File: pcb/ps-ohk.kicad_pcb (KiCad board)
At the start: 2 copper layers, 17 parts, among them IC1 CH552G

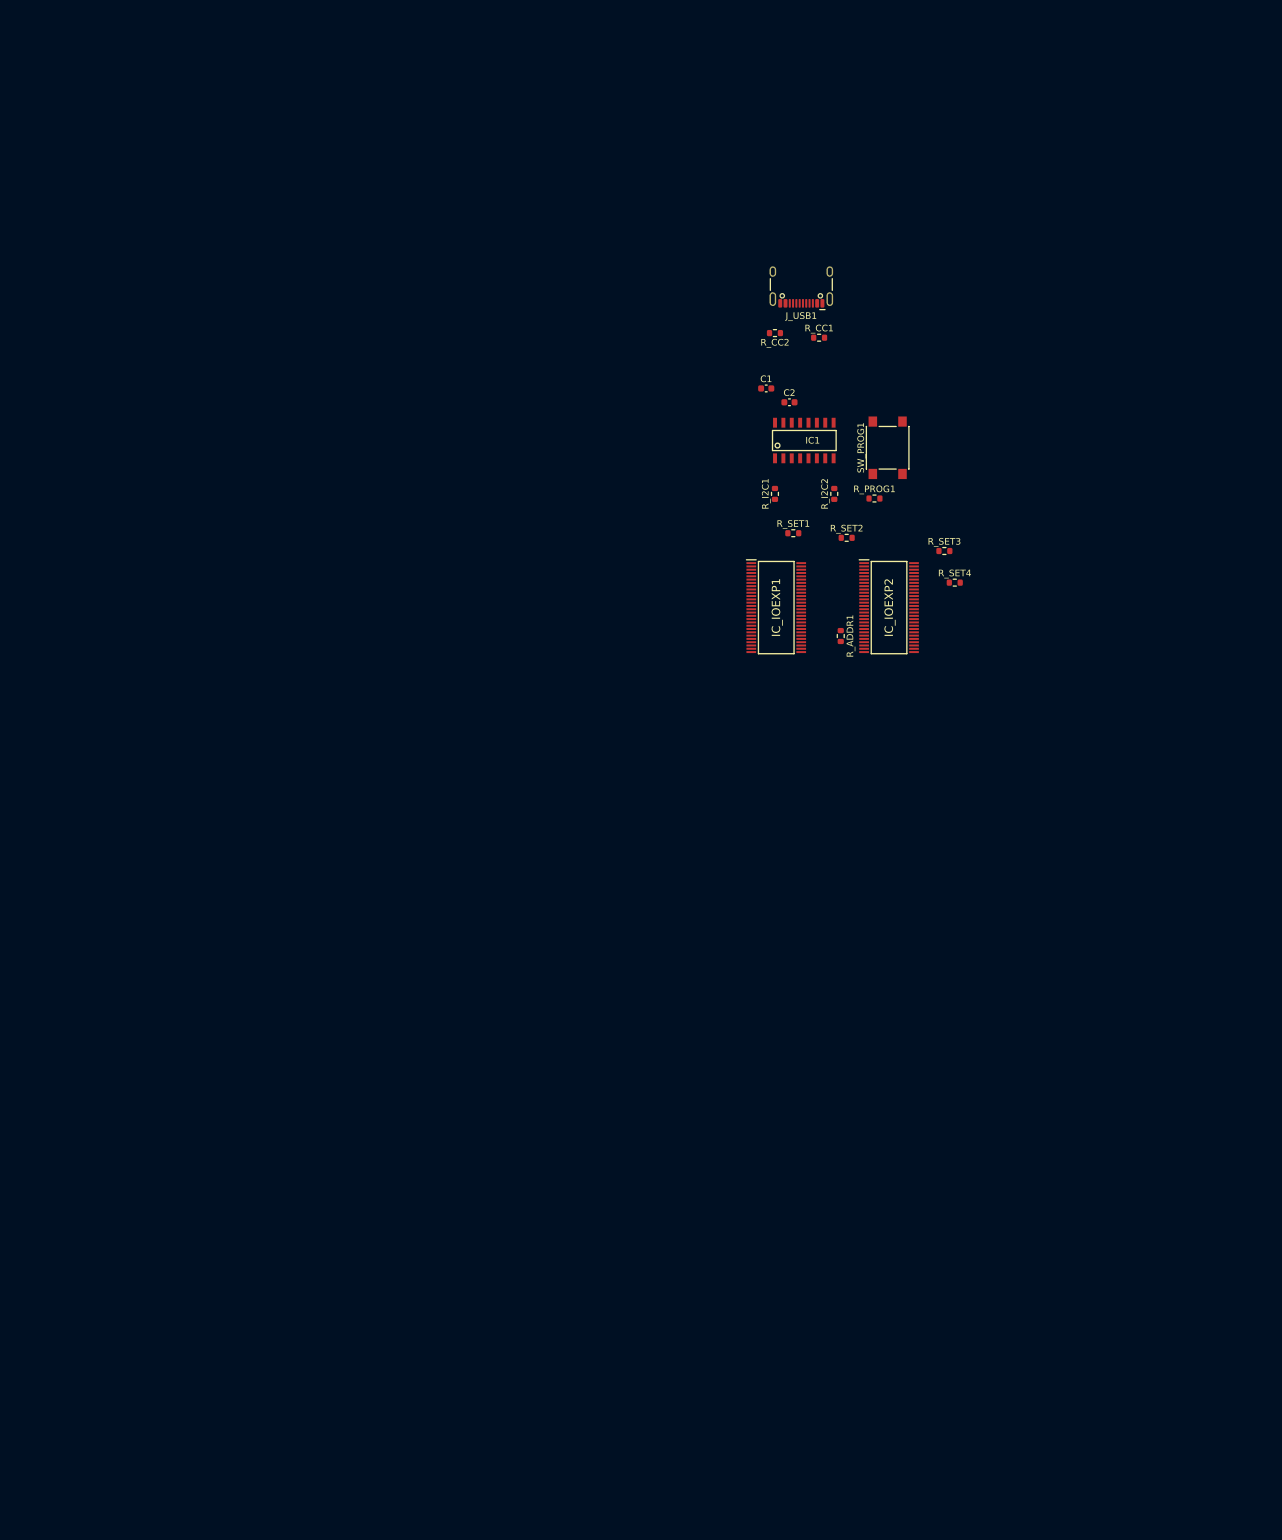
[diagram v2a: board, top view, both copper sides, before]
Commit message: pcb: add buttons and route
Signed-off-by: Dylan Turner <dylan.turner@tutanota.com>
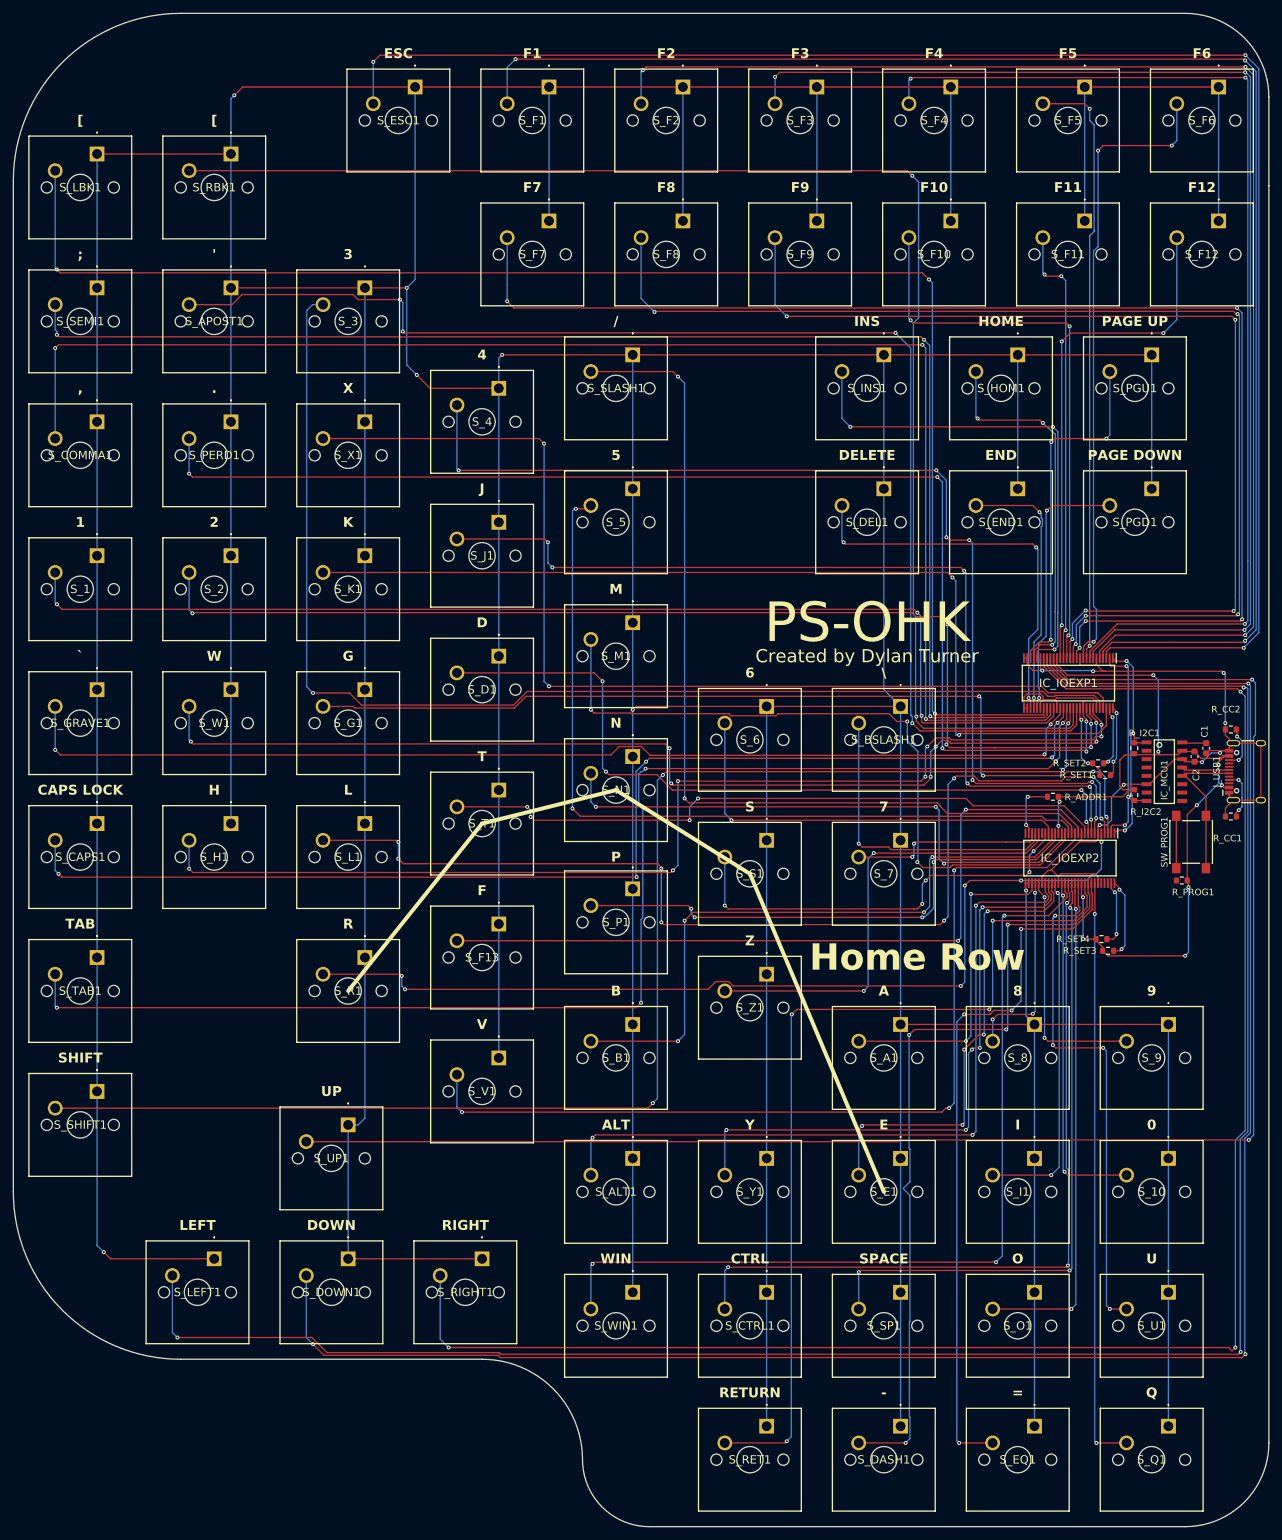
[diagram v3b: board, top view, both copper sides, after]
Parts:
- added S_1: ~, COM-13834:COM13834, F.Cu at (27.9, 81.3)
- added S_10: ~, COM-13834:COM13834, F.Cu at (190.5, 172.7)
- added S_2: ~, COM-13834:COM13834, F.Cu at (48.3, 81.3)
- added S_3: ~, COM-13834:COM13834, F.Cu at (68.6, 40.6)
- added S_4: ~, COM-13834:COM13834, F.Cu at (88.9, 55.9)
- added S_5: ~, COM-13834:COM13834, F.Cu at (109.2, 71.1)
- added S_6: ~, COM-13834:COM13834, F.Cu at (129.5, 104.1)
- added S_7: ~, COM-13834:COM13834, F.Cu at (149.9, 124.5)
- added S_8: ~, COM-13834:COM13834, F.Cu at (170.2, 152.4)
- added S_9: ~, COM-13834:COM13834, F.Cu at (190.5, 152.4)
- added S_A1: ~, COM-13834:COM13834, F.Cu at (149.9, 152.4)
- added S_ALT1: ~, COM-13834:COM13834, F.Cu at (109.2, 172.7)
- added S_APOST1: ~, COM-13834:COM13834, F.Cu at (48.3, 40.6)
- added S_B1: ~, COM-13834:COM13834, F.Cu at (109.2, 152.4)
- added S_BSLASH1: ~, COM-13834:COM13834, F.Cu at (149.9, 104.1)
- added S_CAPS1: ~, COM-13834:COM13834, F.Cu at (27.9, 121.9)
- added S_COMMA1: ~, COM-13834:COM13834, F.Cu at (27.9, 61.0)
- added S_CTRL1: ~, COM-13834:COM13834, F.Cu at (129.5, 193.0)
- added S_D1: ~, COM-13834:COM13834, F.Cu at (88.9, 96.5)
- added S_DASH1: ~, COM-13834:COM13834, F.Cu at (149.9, 213.4)
- added S_DEL1: ~, COM-13834:COM13834, F.Cu at (147.3, 71.1)
- added S_DOWN1: ~, COM-13834:COM13834, F.Cu at (66.0, 188.0)
- added S_E1: ~, COM-13834:COM13834, F.Cu at (149.9, 172.7)
- added S_END1: ~, COM-13834:COM13834, F.Cu at (167.6, 71.1)
- added S_EQ1: ~, COM-13834:COM13834, F.Cu at (170.2, 213.4)
- added S_ESC1: ~, COM-13834:COM13834, F.Cu at (76.2, 10.2)
- added S_F1: ~, COM-13834:COM13834, F.Cu at (96.5, 10.2)
- added S_F10: ~, COM-13834:COM13834, F.Cu at (157.5, 30.5)
- added S_F11: ~, COM-13834:COM13834, F.Cu at (177.8, 30.5)
- added S_F12: ~, COM-13834:COM13834, F.Cu at (198.1, 30.5)
- added S_F13: ~, COM-13834:COM13834, F.Cu at (88.9, 137.2)
- added S_F2: ~, COM-13834:COM13834, F.Cu at (116.8, 10.2)
- added S_F3: ~, COM-13834:COM13834, F.Cu at (137.2, 10.2)
- added S_F4: ~, COM-13834:COM13834, F.Cu at (157.5, 10.2)
- added S_F5: ~, COM-13834:COM13834, F.Cu at (177.8, 10.2)
- added S_F6: ~, COM-13834:COM13834, F.Cu at (198.1, 10.2)
- added S_F7: ~, COM-13834:COM13834, F.Cu at (96.5, 30.5)
- added S_F8: ~, COM-13834:COM13834, F.Cu at (116.8, 30.5)
- added S_F9: ~, COM-13834:COM13834, F.Cu at (137.2, 30.5)
- added S_G1: ~, COM-13834:COM13834, F.Cu at (68.6, 101.6)
- added S_GRAVE1: ~, COM-13834:COM13834, F.Cu at (27.9, 101.6)
- added S_H1: ~, COM-13834:COM13834, F.Cu at (48.3, 121.9)
- added S_HOM1: ~, COM-13834:COM13834, F.Cu at (167.6, 50.8)
- added S_I1: ~, COM-13834:COM13834, F.Cu at (170.2, 172.7)
- added S_INS1: ~, COM-13834:COM13834, F.Cu at (147.3, 50.8)
- added S_J1: ~, COM-13834:COM13834, F.Cu at (88.9, 76.2)
- added S_K1: ~, COM-13834:COM13834, F.Cu at (68.6, 81.3)
- added S_L1: ~, COM-13834:COM13834, F.Cu at (68.6, 121.9)
- added S_LBK1: ~, COM-13834:COM13834, F.Cu at (27.9, 20.3)
- added S_LEFT1: ~, COM-13834:COM13834, F.Cu at (45.7, 188.0)
- added S_M1: ~, COM-13834:COM13834, F.Cu at (109.2, 91.4)
- added S_N1: ~, COM-13834:COM13834, F.Cu at (109.2, 111.8)
- added S_O1: ~, COM-13834:COM13834, F.Cu at (170.2, 193.0)
- added S_P1: ~, COM-13834:COM13834, F.Cu at (109.2, 131.8)
- added S_PERD1: ~, COM-13834:COM13834, F.Cu at (48.3, 61.0)
- added S_PGD1: ~, COM-13834:COM13834, F.Cu at (188.0, 71.1)
- added S_PGU1: ~, COM-13834:COM13834, F.Cu at (188.0, 50.8)
- added S_Q1: ~, COM-13834:COM13834, F.Cu at (190.5, 213.4)
- added S_R1: ~, COM-13834:COM13834, F.Cu at (68.6, 142.2)
- added S_RBK1: ~, COM-13834:COM13834, F.Cu at (48.3, 20.3)
- added S_RET1: ~, COM-13834:COM13834, F.Cu at (129.5, 213.4)
- added S_RIGHT1: ~, COM-13834:COM13834, F.Cu at (86.4, 188.0)
- added S_S1: ~, COM-13834:COM13834, F.Cu at (129.5, 124.5)
- added S_SEMI1: ~, COM-13834:COM13834, F.Cu at (27.9, 40.6)
- added S_SHIFT1: ~, COM-13834:COM13834, F.Cu at (27.9, 162.6)
- added S_SLASH1: ~, COM-13834:COM13834, F.Cu at (109.2, 50.8)
- added S_SP1: ~, COM-13834:COM13834, F.Cu at (149.9, 193.0)
- added S_T1: ~, COM-13834:COM13834, F.Cu at (88.9, 116.8)
- added S_TAB1: ~, COM-13834:COM13834, F.Cu at (27.9, 142.2)
- added S_U1: ~, COM-13834:COM13834, F.Cu at (190.5, 193.0)
- added S_UP1: ~, COM-13834:COM13834, F.Cu at (66.0, 167.6)
- added S_V1: ~, COM-13834:COM13834, F.Cu at (88.9, 157.5)
- added S_W1: ~, COM-13834:COM13834, F.Cu at (48.3, 101.6)
- added S_WIN1: ~, COM-13834:COM13834, F.Cu at (109.2, 193.0)
- added S_X1: ~, COM-13834:COM13834, F.Cu at (68.6, 61.0)
- added S_Y1: ~, COM-13834:COM13834, F.Cu at (129.5, 172.7)
- added S_Z1: ~, COM-13834:COM13834, F.Cu at (129.5, 144.8)
- IC_IOEXP1, IC_IOEXP2: value PCA9505DGGY -> ~
- IC_MCU1: renamed from IC1; value CH552G -> ~
- moved J_USB1 101.5 mm to (203.5, 114.0), turned to 90 degrees
- moved R_CC1 95.8 mm to (200.0, 120.9), turned to 180 degrees
- moved R_CC2 91.7 mm to (200.0, 107.6)
- moved C1 86.2 mm to (196.2, 110.5), turned to -90 degrees
- moved C2 81.7 mm to (194.5, 111.8), turned to -90 degrees
- moved SW_PROG1 75.5 mm to (193.9, 124.7)
- moved R_PROG1 74.4 mm to (192.5, 130.6), turned to 180 degrees
- moved IC_MCU1 74.2 mm to (189.9, 114.0), turned to 0 degrees
- moved R_I2C1 66.8 mm to (185.3, 110.5)
- moved R_SET3 65.6 mm to (181.4, 141.2)
- moved R_I2C2 64.5 mm to (185.3, 117.6), turned to -90 degrees
- moved R_SET1 59.9 mm to (180.9, 114.6)
- moved R_SET4 58.5 mm to (180.3, 139.4)
- moved R_SET2 51.2 mm to (179.8, 112.8)
- moved IC_IOEXP2 46.9 mm to (175.6, 127.2), turned to -90 degrees
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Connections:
- IC_IOEXP1 pad 10: unconnected-(IC_IOEXP1-IO0_6-Pad10) -> /KEY_F6
- IC_IOEXP1 pad 12: unconnected-(IC_IOEXP1-IO0_7-Pad12) -> /KEY_F7
- IC_IOEXP1 pad 13: unconnected-(IC_IOEXP1-IO1_0-Pad13) -> /KEY_F8
- IC_IOEXP1 pad 14: unconnected-(IC_IOEXP1-IO1_1-Pad14) -> /KEY_F9
- IC_IOEXP1 pad 15: unconnected-(IC_IOEXP1-IO1_2-Pad15) -> /KEY_F10
- IC_IOEXP1 pad 16: unconnected-(IC_IOEXP1-IO1_3-Pad16) -> /KEY_F11
- IC_IOEXP1 pad 17: unconnected-(IC_IOEXP1-IO1_4-Pad17) -> /KEY_F12
- IC_IOEXP1 pad 19: unconnected-(IC_IOEXP1-IO1_5-Pad19) -> /KEY_UP
- IC_IOEXP1 pad 20: unconnected-(IC_IOEXP1-IO1_6-Pad20) -> /KEY_DOWN
- IC_IOEXP1 pad 21: unconnected-(IC_IOEXP1-IO1_7-Pad21) -> /KEY_LEFT
- IC_IOEXP1 pad 22: unconnected-(IC_IOEXP1-IO2_0-Pad22) -> /KEY_RIGHT
- IC_IOEXP1 pad 24: unconnected-(IC_IOEXP1-IO2_1-Pad24) -> /KEY_INS
- IC_IOEXP1 pad 25: unconnected-(IC_IOEXP1-IO2_2-Pad25) -> /KEY_HOM
- IC_IOEXP1 pad 26: unconnected-(IC_IOEXP1-IO2_3-Pad26) -> /KEY_PGU
- IC_IOEXP1 pad 3: /KEY_A -> /KEY_ESC
- IC_IOEXP1 pad 31: unconnected-(IC_IOEXP1-IO2_4-Pad31) -> /KEY_DEL
- IC_IOEXP1 pad 32: unconnected-(IC_IOEXP1-IO2_5-Pad32) -> /KEY_END
- IC_IOEXP1 pad 33: unconnected-(IC_IOEXP1-IO2_6-Pad33) -> /KEY_PGD
- IC_IOEXP1 pad 35: unconnected-(IC_IOEXP1-IO2_7-Pad35) -> /KEY_LBK
- IC_IOEXP1 pad 36: unconnected-(IC_IOEXP1-IO3_0-Pad36) -> /KEY_SEMI
- IC_IOEXP1 pad 37: unconnected-(IC_IOEXP1-IO3_1-Pad37) -> /KEY_COMMA
- IC_IOEXP1 pad 38: unconnected-(IC_IOEXP1-IO3_2-Pad38) -> /KEY_1
- IC_IOEXP1 pad 4: unconnected-(IC_IOEXP1-IO0_1-Pad4) -> /KEY_F1
- IC_IOEXP1 pad 40: unconnected-(IC_IOEXP1-IO3_3-Pad40) -> /KEY_GRAVE
- IC_IOEXP1 pad 41: unconnected-(IC_IOEXP1-IO3_4-Pad41) -> /KEY_CAPS
- IC_IOEXP1 pad 42: unconnected-(IC_IOEXP1-IO3_5-Pad42) -> /KEY_TAB
- IC_IOEXP1 pad 43: unconnected-(IC_IOEXP1-IO3_6-Pad43) -> /KEY_SHIFT
- IC_IOEXP1 pad 44: unconnected-(IC_IOEXP1-IO3_7-Pad44) -> /KEY_RBK
- IC_IOEXP1 pad 45: unconnected-(IC_IOEXP1-IO4_0-Pad45) -> /KEY_APOST
- IC_IOEXP1 pad 47: unconnected-(IC_IOEXP1-IO4_1-Pad47) -> /KEY_PERD
- IC_IOEXP1 pad 48: unconnected-(IC_IOEXP1-IO4_2-Pad48) -> /KEY_2
- IC_IOEXP1 pad 49: unconnected-(IC_IOEXP1-IO4_3-Pad49) -> /KEY_W
- IC_IOEXP1 pad 5: unconnected-(IC_IOEXP1-IO0_2-Pad5) -> /KEY_F2
- IC_IOEXP1 pad 50: unconnected-(IC_IOEXP1-IO4_4-Pad50) -> /KEY_H
- IC_IOEXP1 pad 52: unconnected-(IC_IOEXP1-IO4_5-Pad52) -> /KEY_3
- IC_IOEXP1 pad 53: unconnected-(IC_IOEXP1-IO4_6-Pad53) -> /KEY_X
- IC_IOEXP1 pad 54: unconnected-(IC_IOEXP1-IO4_7-Pad54) -> /KEY_K
- IC_IOEXP1 pad 7: unconnected-(IC_IOEXP1-IO0_3-Pad7) -> /KEY_F3
- IC_IOEXP1 pad 8: unconnected-(IC_IOEXP1-IO0_4-Pad8) -> /KEY_F4
- IC_IOEXP1 pad 9: unconnected-(IC_IOEXP1-IO0_5-Pad9) -> /KEY_F5
- IC_IOEXP2 pad 10: unconnected-(IC_IOEXP2-IO0_6-Pad10) -> /KEY_T
- IC_IOEXP2 pad 12: unconnected-(IC_IOEXP2-IO0_7-Pad12) -> /KEY_F
- IC_IOEXP2 pad 13: unconnected-(IC_IOEXP2-IO1_0-Pad13) -> /KEY_V
- IC_IOEXP2 pad 14: unconnected-(IC_IOEXP2-IO1_1-Pad14) -> /KEY_SLASH
- IC_IOEXP2 pad 15: unconnected-(IC_IOEXP2-IO1_2-Pad15) -> /KEY_5
- IC_IOEXP2 pad 16: unconnected-(IC_IOEXP2-IO1_3-Pad16) -> /KEY_M
- IC_IOEXP2 pad 17: unconnected-(IC_IOEXP2-IO1_4-Pad17) -> /KEY_N
- IC_IOEXP2 pad 19: unconnected-(IC_IOEXP2-IO1_5-Pad19) -> /KEY_P
- IC_IOEXP2 pad 20: unconnected-(IC_IOEXP2-IO1_6-Pad20) -> /KEY_B
- IC_IOEXP2 pad 21: unconnected-(IC_IOEXP2-IO1_7-Pad21) -> /KEY_6
- IC_IOEXP2 pad 22: unconnected-(IC_IOEXP2-IO2_0-Pad22) -> /KEY_S
- IC_IOEXP2 pad 24: unconnected-(IC_IOEXP2-IO2_1-Pad24) -> /KEY_Z
- IC_IOEXP2 pad 25: unconnected-(IC_IOEXP2-IO2_2-Pad25) -> /KEY_BSLASH
- IC_IOEXP2 pad 26: unconnected-(IC_IOEXP2-IO2_3-Pad26) -> /KEY_7
- IC_IOEXP2 pad 3: unconnected-(IC_IOEXP2-IO0_0-Pad3) -> /KEY_G
- IC_IOEXP2 pad 31: unconnected-(IC_IOEXP2-IO2_4-Pad31) -> /KEY_A
- IC_IOEXP2 pad 32: unconnected-(IC_IOEXP2-IO2_5-Pad32) -> /KEY_8
- IC_IOEXP2 pad 33: unconnected-(IC_IOEXP2-IO2_6-Pad33) -> /KEY_9
- IC_IOEXP2 pad 35: unconnected-(IC_IOEXP2-IO2_7-Pad35) -> /KEY_ALT
- IC_IOEXP2 pad 36: unconnected-(IC_IOEXP2-IO3_0-Pad36) -> /KEY_Y
- IC_IOEXP2 pad 37: unconnected-(IC_IOEXP2-IO3_1-Pad37) -> /KEY_E
- IC_IOEXP2 pad 38: unconnected-(IC_IOEXP2-IO3_2-Pad38) -> /KEY_I
- IC_IOEXP2 pad 4: unconnected-(IC_IOEXP2-IO0_1-Pad4) -> /KEY_L
- IC_IOEXP2 pad 40: unconnected-(IC_IOEXP2-IO3_3-Pad40) -> /KEY_0
- IC_IOEXP2 pad 41: unconnected-(IC_IOEXP2-IO3_4-Pad41) -> /KEY_WIN
- IC_IOEXP2 pad 42: unconnected-(IC_IOEXP2-IO3_5-Pad42) -> /KEY_CTRL
- IC_IOEXP2 pad 43: unconnected-(IC_IOEXP2-IO3_6-Pad43) -> /KEY_SP
- IC_IOEXP2 pad 44: unconnected-(IC_IOEXP2-IO3_7-Pad44) -> /KEY_O
- IC_IOEXP2 pad 45: unconnected-(IC_IOEXP2-IO4_0-Pad45) -> /KEY_U
- IC_IOEXP2 pad 47: unconnected-(IC_IOEXP2-IO4_1-Pad47) -> /KEY_RET
- IC_IOEXP2 pad 48: unconnected-(IC_IOEXP2-IO4_2-Pad48) -> /KEY_DASH
- IC_IOEXP2 pad 49: unconnected-(IC_IOEXP2-IO4_3-Pad49) -> /KEY_EQ
- IC_IOEXP2 pad 5: unconnected-(IC_IOEXP2-IO0_2-Pad5) -> /KEY_R
- IC_IOEXP2 pad 50: unconnected-(IC_IOEXP2-IO4_4-Pad50) -> /KEY_Q
- IC_IOEXP2 pad 7: unconnected-(IC_IOEXP2-IO0_3-Pad7) -> /KEY_4
- IC_IOEXP2 pad 8: unconnected-(IC_IOEXP2-IO0_4-Pad8) -> /KEY_J
- IC_IOEXP2 pad 9: unconnected-(IC_IOEXP2-IO0_5-Pad9) -> /KEY_D
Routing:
- net GND: track 0.00 -> 1876.6 mm, vias 0 -> 15
- net /KEY_LEFT: track 0.00 -> 306.5 mm, vias 0 -> 3
- net /KEY_DOWN: track 0.00 -> 288.0 mm, vias 0 -> 3
- net /KEY_RIGHT: track 0.00 -> 264.4 mm, vias 0 -> 3
- net /KEY_ESC: track 0.00 -> 252.9 mm, vias 0 -> 3
- net /KEY_UP: track 0.00 -> 245.7 mm, vias 0 -> 2
- net /KEY_LBK: track 0.00 -> 231.9 mm, vias 0 -> 3
- net /KEY_F1: track 0.00 -> 230.8 mm, vias 0 -> 3
- net /KEY_COMMA: track 0.00 -> 223.6 mm, vias 0 -> 3
- net /KEY_RBK: track 0.00 -> 220.7 mm, vias 0 -> 2
- net /KEY_SEMI: track 0.00 -> 213.1 mm, vias 0 -> 3
- net /KEY_SHIFT: track 0.00 -> 212.3 mm, vias 0 -> 4
- net /KEY_F2: track 0.00 -> 208.3 mm, vias 0 -> 3
- net /KEY_TAB: track 0.00 -> 202.0 mm, vias 0 -> 5
- net /KEY_APOST: track 0.00 -> 201.4 mm, vias 0 -> 4
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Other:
- board outline added: 190.5 x 229.6 mm
- board text added: "'"
- board text added: ","
- board text added: "-"
- board text added: "."
- board text added: "/"
- board text added: "0"
- board text added: "1"
- board text added: "2"
- board text added: "3"
- board text added: "4"
- board text added: "5"
- board text added: "6"
- board text added: "7"
- board text added: "8"
- board text added: "9"
- board text added: ";"
- board text added: "="
- board text added: "A"
- board text added: "ALT"
- board text added: "B"
- board text added: "CAPS LOCK"
- board text added: "CTRL"
- board text added: "Created by Dylan Turner"
- board text added: "D"
- board text added: "DELETE"
- board text added: "DOWN"
- board text added: "E"
- board text added: "END"
- board text added: "ESC"
- board text added: "F"
- board text added: "F1"
- board text added: "F10"
- board text added: "F11"
- board text added: "F12"
- board text added: "F2"
- board text added: "F3"
- board text added: "F4"
- board text added: "F5"
- board text added: "F6"
- board text added: "F7"
- board text added: "F8"
- board text added: "F9"
- board text added: "G"
- board text added: "H"
- board text added: "HOME"
- board text added: "Home Row"
- board text added: "I"
- board text added: "INS"
- board text added: "J"
- board text added: "K"
- board text added: "L"
- board text added: "LEFT"
- board text added: "M"
- board text added: "N"
- board text added: "O"
- board text added: "P"
- board text added: "PAGE DOWN"
- board text added: "PAGE UP"
- board text added: "PS-OHK"
- board text added: "Q"
- board text added: "R"
- board text added: "RETURN"
- board text added: "RIGHT"
- board text added: "S"
- board text added: "SHIFT"
- board text added: "SPACE"
- board text added: "T"
- board text added: "TAB"
- board text added: "U"
- board text added: "UP"
- board text added: "V"
- board text added: "W"
- board text added: "WIN"
- board text added: "X"
- board text added: "Y"
- board text added: "Z"
- board text added: "["
- board text added: "\"
- board text added: "`"

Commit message: pcb: made orderable on pcb-way
Signed-off-by: Dylan Turner <dylan.turner@tutanota.com>
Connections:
- J_USB1 pad B6: unconnected-(J_USB1-D+-PadB6) -> /USB+
- J_USB1 pad B7: unconnected-(J_USB1-D--PadB7) -> /USB-
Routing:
- net /USB-: track 7.28 -> 11.8 mm, vias 0 -> 2
- net /USB+: track 23.1 -> 25.7 mm

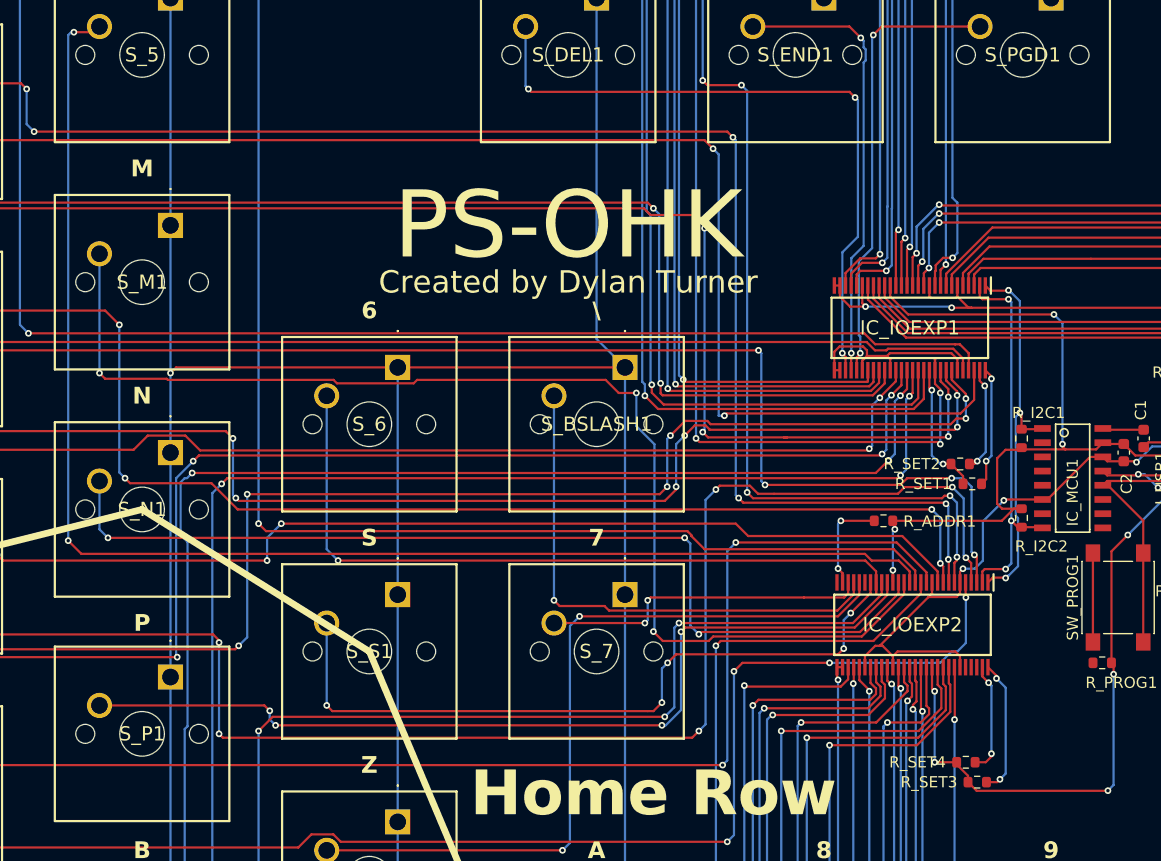
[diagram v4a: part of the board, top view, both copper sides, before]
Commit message: pcb: added C and rmd unneeded hardware
Signed-off-by: Dylan Turner <dylan.turner@tutanota.com>
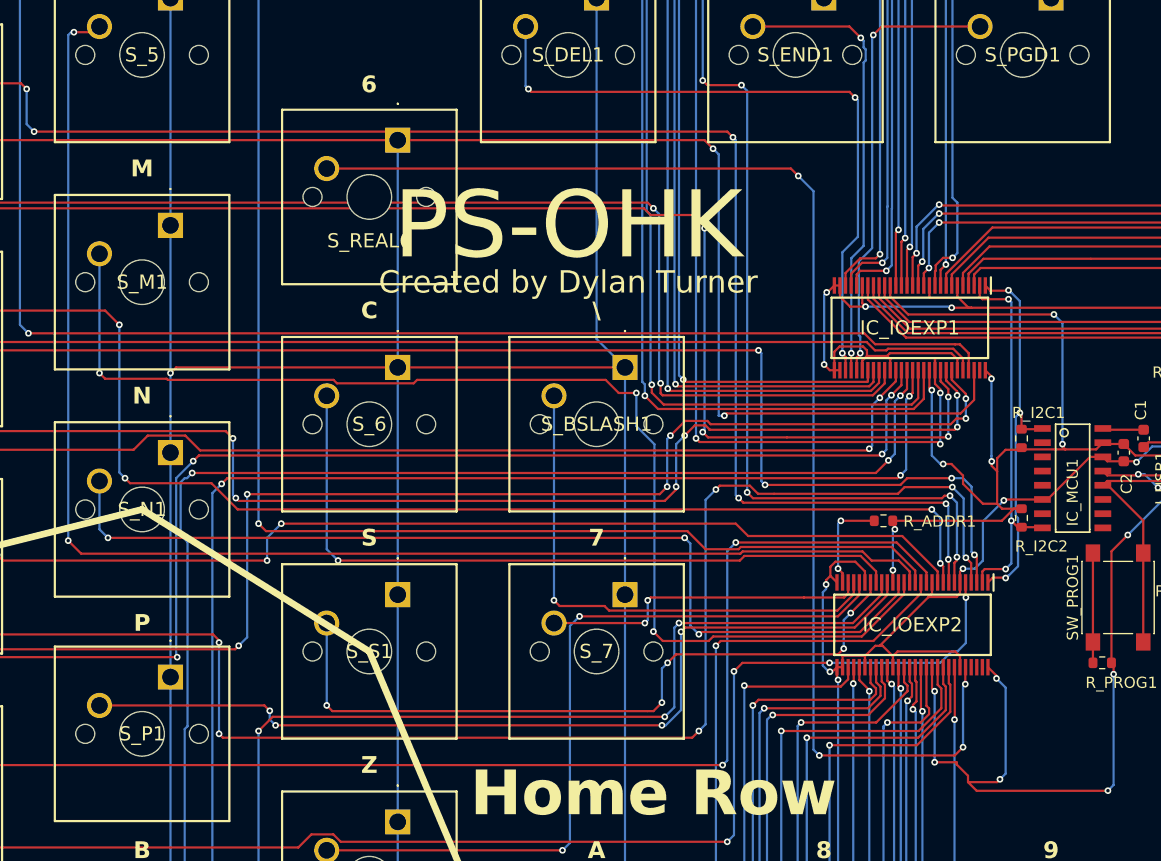
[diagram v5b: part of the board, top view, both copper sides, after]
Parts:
- removed R_SET1, R_SET2, R_SET3, R_SET4: 1-10k, Resistor_SMD:R_0603_1608Metric
- added S_REAL6: ~, COM-13834:COM13834, F.Cu at (129.5, 83.8)
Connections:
- IC_IOEXP1 pad 55: Net-(IC_IOEXP1-~{INT}) -> unconnected-(IC_IOEXP1-~{INT}-Pad55)
- IC_IOEXP1 pad 56: Net-(IC_IOEXP1-~{RESET}) -> VCC
- IC_IOEXP2 pad 52: unconnected-(IC_IOEXP2-IO4_5-Pad52) -> /KEY_REAL_6
- IC_IOEXP2 pad 55: Net-(IC_IOEXP2-~{INT}) -> unconnected-(IC_IOEXP2-~{INT}-Pad55)
- IC_IOEXP2 pad 56: Net-(IC_IOEXP2-~{RESET}) -> VCC
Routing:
- net /KEY_REAL_6: track 0.00 -> 115.4 mm, vias 0 -> 4
- net GND: track 1876.6 -> 1924.8 mm, vias 15 -> 19
- net VCC: track 144.5 -> 171.6 mm, vias 13 -> 17
- net Net-(IC_IOEXP2-~{RESET}): track 12.2 -> 0.00 mm, vias 2 -> 0
- net Net-(IC_IOEXP1-~{RESET}): track 10.8 -> 0.00 mm, vias 2 -> 0
- net Net-(IC_IOEXP2-~{INT}): track 10.0 -> 0.00 mm, vias 2 -> 0
- net Net-(IC_IOEXP1-~{INT}): track 9.47 -> 0.00 mm, vias 2 -> 0
- net Net-(R_PROG1-Pad2): track 7.95 -> 9.82 mm
- net /KEY_6: track 66.6 -> 65.0 mm
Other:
- board text added: "C"
